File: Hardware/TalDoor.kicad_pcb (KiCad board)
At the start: 2 copper layers, 58 parts, among them J1 SI-52003-F_RJ45, J2 Screw_Terminal_01x02, J3 Conn_01x06_Male, J4 Conn_01x06_Male, P1 Conn_02x18_Odd_Even, P2 Conn_02x18_Odd_Even, Q1 RK7002BM, Q2 BSS223PWH6327XTSA1, U1 DRV8837, U2 ENC28J60-I/SO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

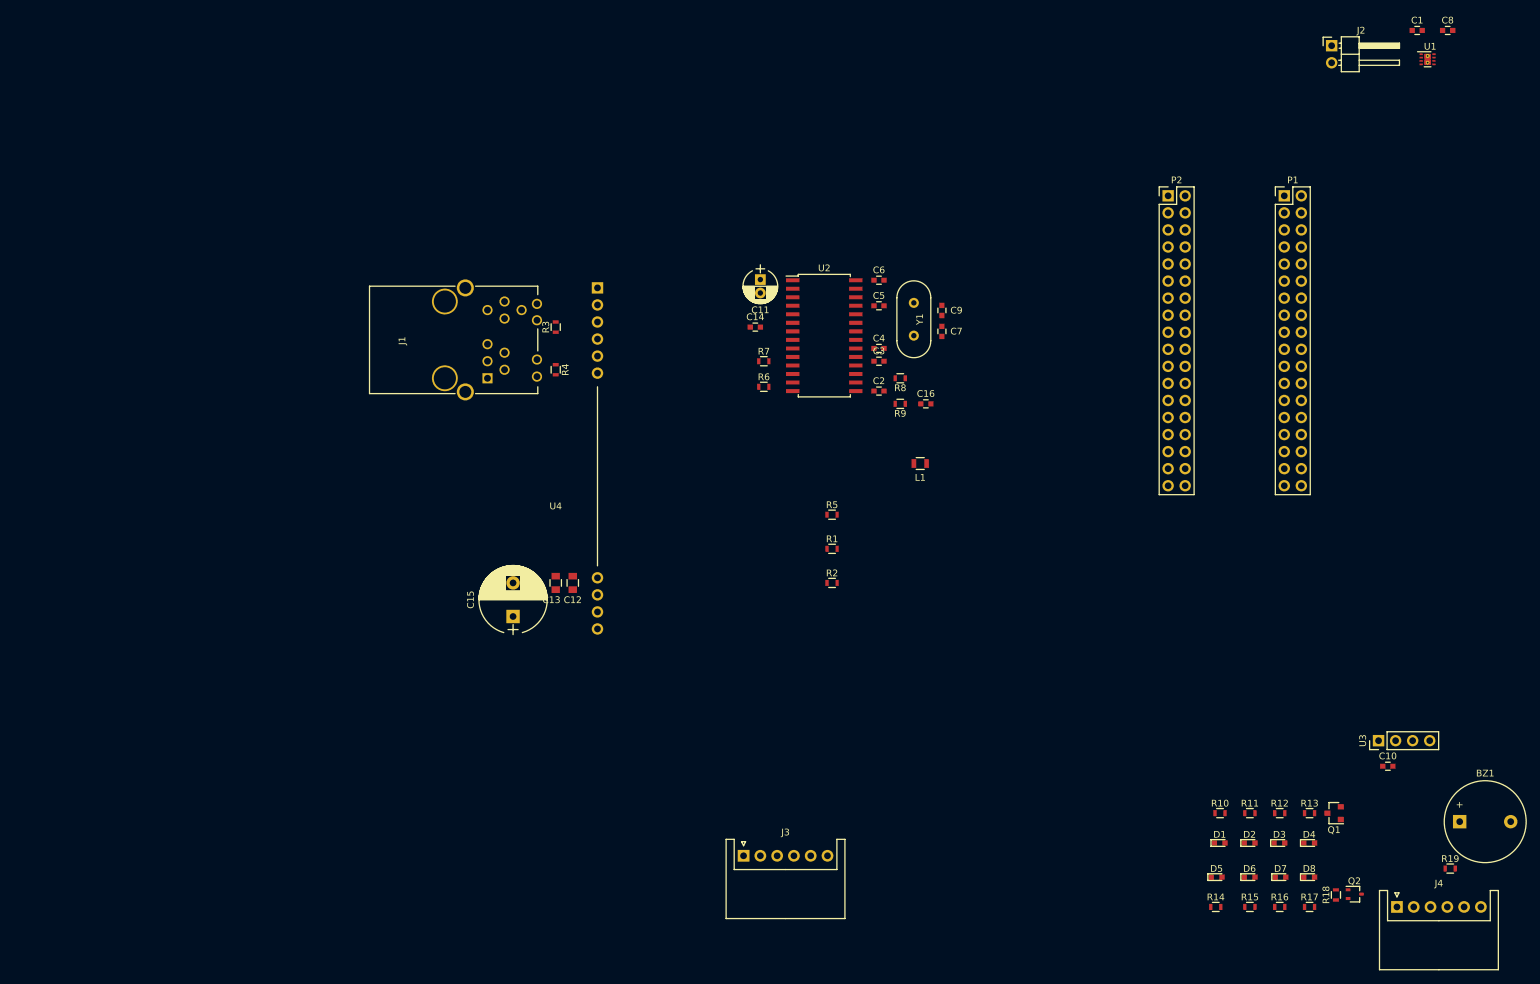
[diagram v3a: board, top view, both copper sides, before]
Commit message: Secondary PCB layout complete
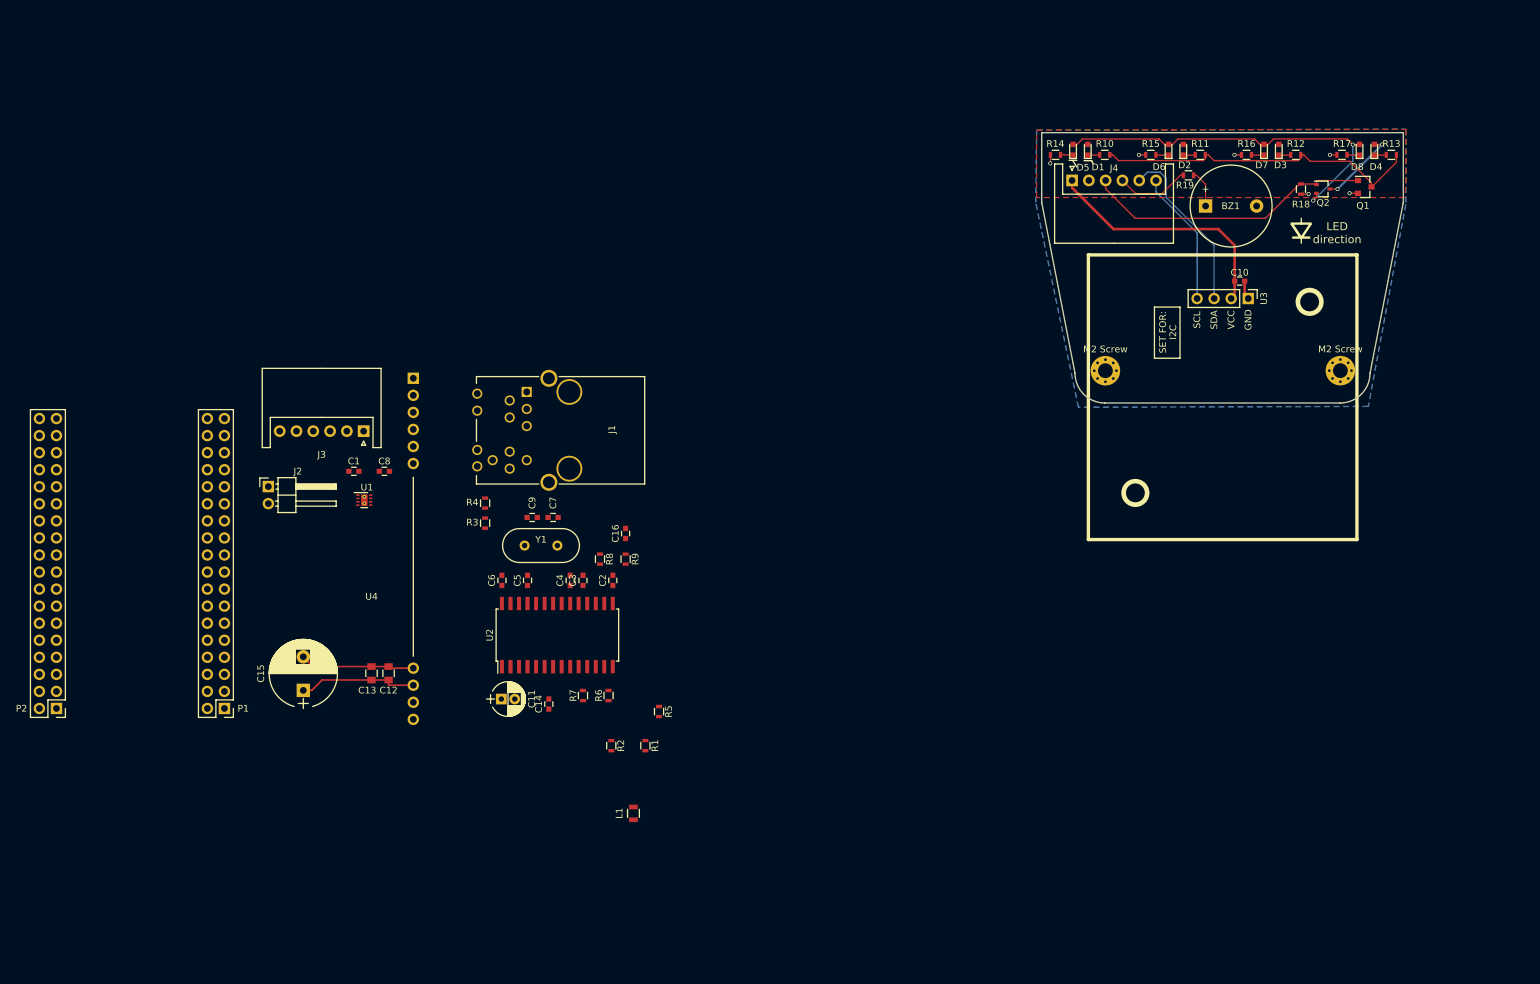
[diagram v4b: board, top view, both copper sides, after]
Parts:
- added M2 Screw: MountingHole_2.2mm_M2_Pad_Via, Mounting_Holes:MountingHole_2.2mm_M2_Pad_Via, F.Cu at (188.6, 70.0)
- added M2 Screw: MountingHole_2.2mm_M2_Pad_Via, Mounting_Holes:MountingHole_2.2mm_M2_Pad_Via, F.Cu at (223.6, 70.0)
- U3: footprint Pin_Headers:Pin_Header_Straight_1x04_Pitch2.54mm -> PN532
- moved P2 182.3 mm to (32.3, 120.3), turned to 180 degrees
- moved P1 175.3 mm to (57.3, 120.3), turned to 180 degrees
- moved C1 171.4 mm to (76.6, 85.0)
- moved C8 171.4 mm to (81.2, 85.0)
- moved J2 171.4 mm to (63.9, 87.2)
- moved U1 171.4 mm to (78.2, 89.3)
- moved J4 118.5 mm to (183.6, 41.7)
- moved R14 114.5 mm to (181.1, 37.8), turned to 180 degrees
- moved R15 113.0 mm to (195.3, 37.8), turned to 180 degrees
- moved R16 112.1 mm to (209.6, 37.8), turned to 180 degrees
- moved R17 112.1 mm to (223.8, 37.8), turned to 180 degrees
- moved D5 110.4 mm to (183.7, 37.1), turned to 90 degrees
- moved R19 110.4 mm to (200.9, 40.9)
- moved D6 109.0 mm to (198.0, 37.1), turned to 90 degrees
- moved D8 108.6 mm to (226.4, 37.1), turned to 90 degrees
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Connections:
- BZ1 pad 2: GND -> /GND2
- C10 pad 1: Net-(C10-Pad1) -> /GND2
- C10 pad 2: Net-(C10-Pad2) -> /+3.3v2
- D1 pad 2: +3V3 -> /+3.3v2
- D2 pad 2: +3V3 -> /+3.3v2
- D3 pad 2: +3V3 -> /+3.3v2
- D4 pad 2: +3V3 -> /+3.3v2
- J4 pad 1: Net-(C10-Pad2) -> /+3.3v2
- J4 pad 2: Net-(C10-Pad1) -> /GND2
- Q1 pad 2: GND -> /GND2
- Q2 pad 3: +3V3 -> /+3.3v2
- R14 pad 2: GND -> /GND2
- R15 pad 2: GND -> /GND2
- R16 pad 2: GND -> /GND2
- R17 pad 2: GND -> /GND2
- R18 pad 1: GND -> /GND2
- U3 pad 1: Net-(C10-Pad1) -> /GND2
- U3 pad 2: Net-(C10-Pad2) -> /+3.3v2
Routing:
- net Net-(D5-Pad2): track 0.00 -> 56.8 mm, vias 0 -> 2
- net Net-(Q1-Pad3): track 0.00 -> 49.7 mm
- net /+3.3v2: track 0.00 -> 48.7 mm, vias 0 -> 2
- net Net-(J4-Pad3): track 0.00 -> 43.3 mm
- net Net-(J4-Pad5): track 0.00 -> 25.8 mm
- net Net-(J4-Pad6): track 0.00 -> 20.1 mm
- net +3V3: track 0.00 -> 17.8 mm
- net GND: track 0.00 -> 17.1 mm
- net Net-(J4-Pad4): track 0.00 -> 11.0 mm
- net /GND2: track 0.00 -> 9.60 mm, vias 0 -> 6
- net Net-(BZ1-Pad1): track 0.00 -> 5.58 mm
- net Net-(D6-Pad1): track 0.00 -> 1.91 mm
- net Net-(D7-Pad1): track 0.00 -> 1.88 mm
- net Net-(D5-Pad1): track 0.00 -> 1.88 mm
- net Net-(D8-Pad1): track 0.00 -> 1.88 mm
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- added copper zone on F.Cu, net /+3.3v2
- added copper zone on B.Cu, net /GND2
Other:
- board outline added: 53.8 x 40.3 mm
- net class Default: trace_width 0.25 -> 0.2
- board text added: "<-- Cut Away inner wall -->"
- board text added: "Box Interior Dimensions"
- board text added: "LED BAR"
- board text added: "LED direction"
- board text added: "PCB Mounting Holes M2"
- board text added: "Pocket Beage Component Side Facing UP"
- board text added: "uUSB"

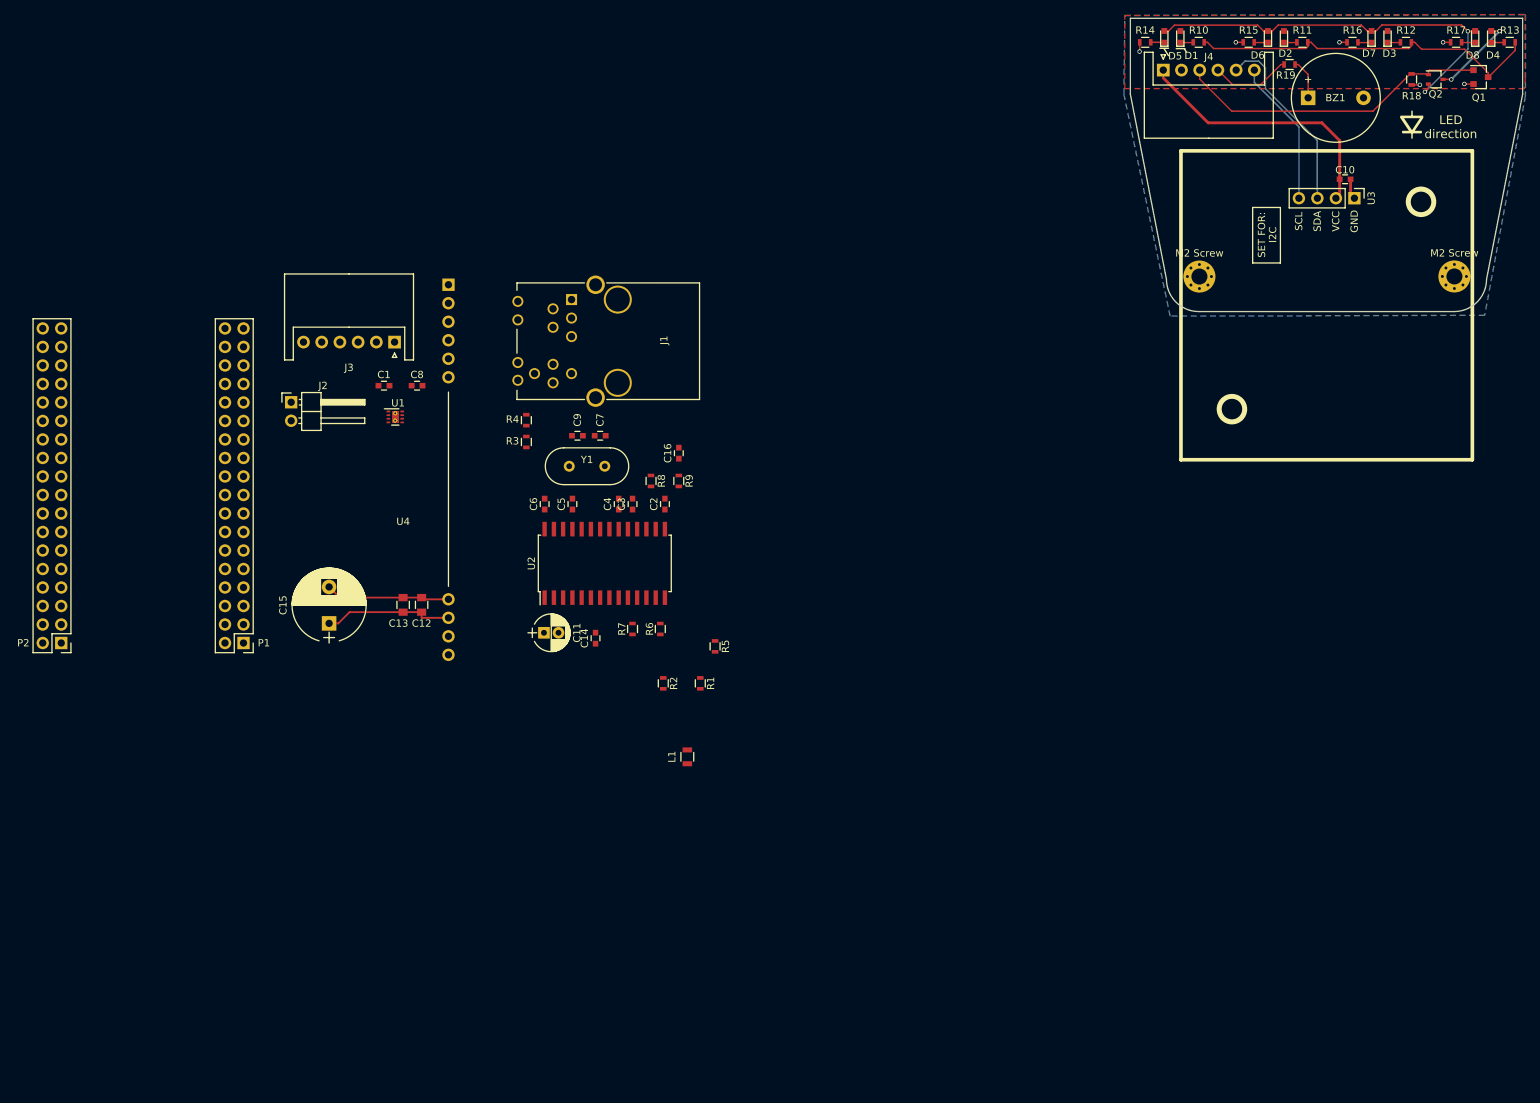
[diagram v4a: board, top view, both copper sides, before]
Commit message: adding measurements for main PCB
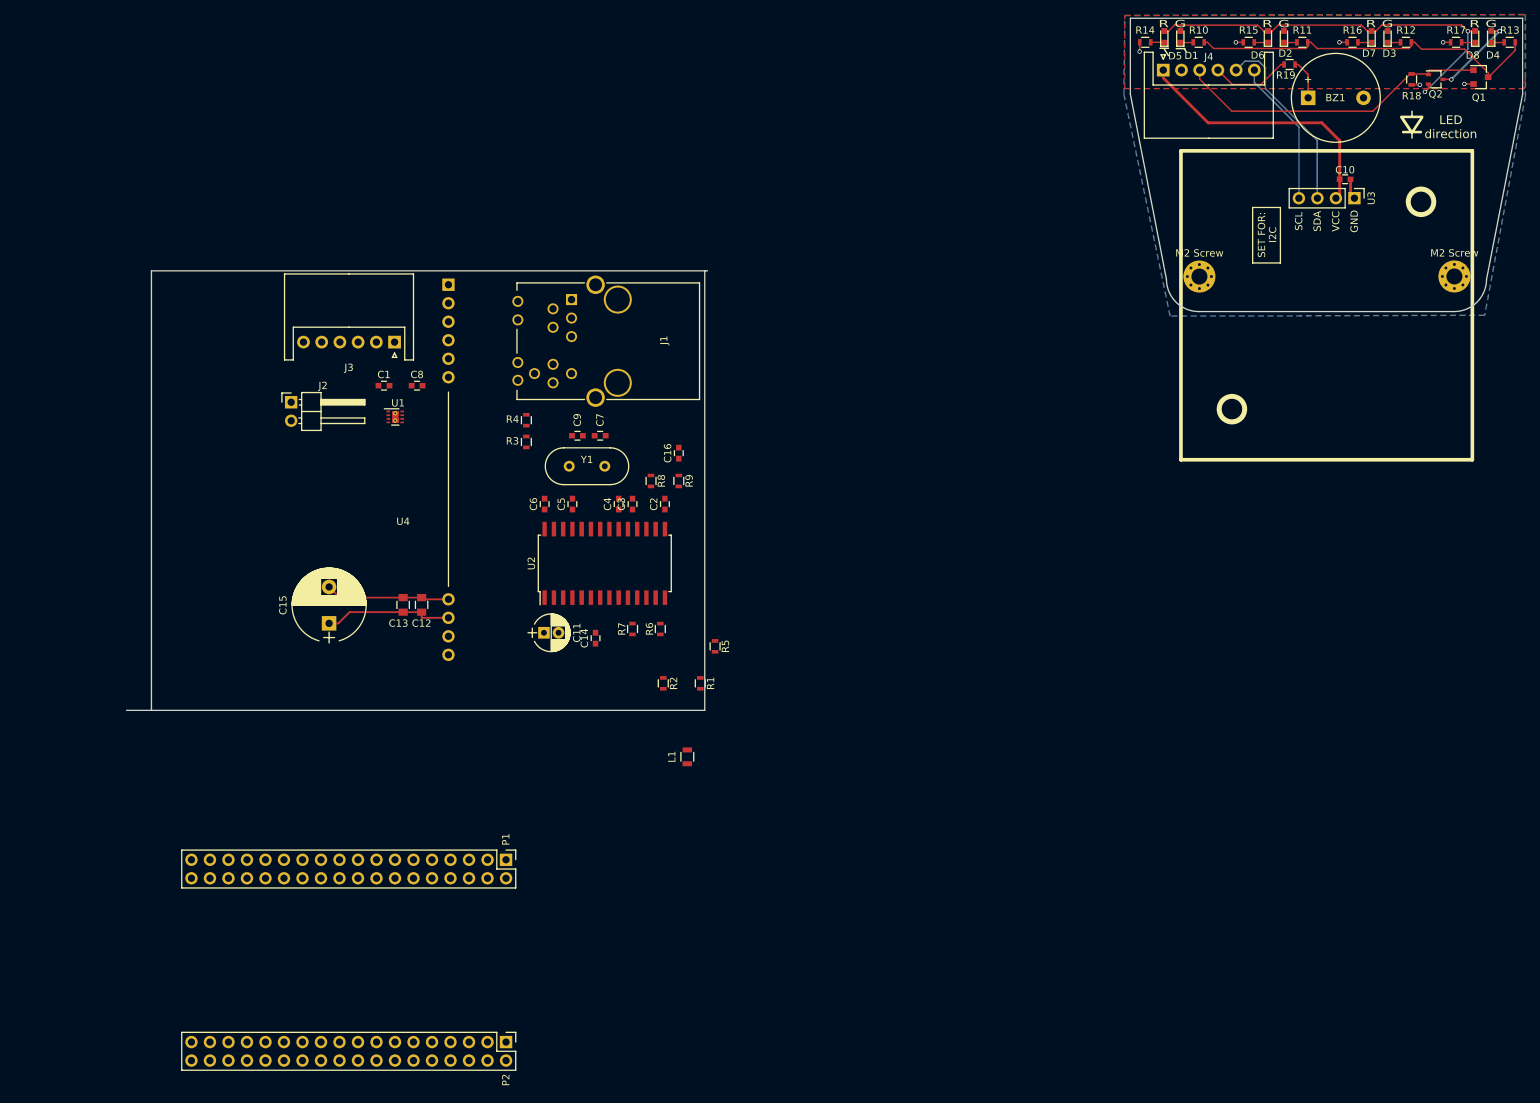
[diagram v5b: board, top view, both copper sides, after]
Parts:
- moved P2 82.0 mm to (93.4, 175.1), turned to 270 degrees
- moved P1 46.7 mm to (93.4, 150.1), turned to 270 degrees
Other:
- board size 53.8 x 40.3 mm -> 191.6 x 95 mm
- board text added: "G"
- board text added: "MAX WIDTH 76mm"
- board text added: "Original Gatekeeper Height 60mm"
- board text added: "R"
- board text added: "RJ40 Bump out 3mm"
